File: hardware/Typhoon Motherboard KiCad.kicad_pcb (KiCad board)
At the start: 2 copper layers, 65.7 x 44.9 mm, 57 parts, among them J1 Conn_01x04_Pin, J10 USB_C_Receptacle_USB2.0, J11 Conn_01x02_Pin, J12 Conn_01x02_Pin, J13 Conn_01x02_Pin, J14 Conn_01x02_Pin, J15 Conn_01x02_Pin, J16 Conn_01x02_Pin, J2 Conn_02x03_Odd_Even, J3 Conn_01x04_Pin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

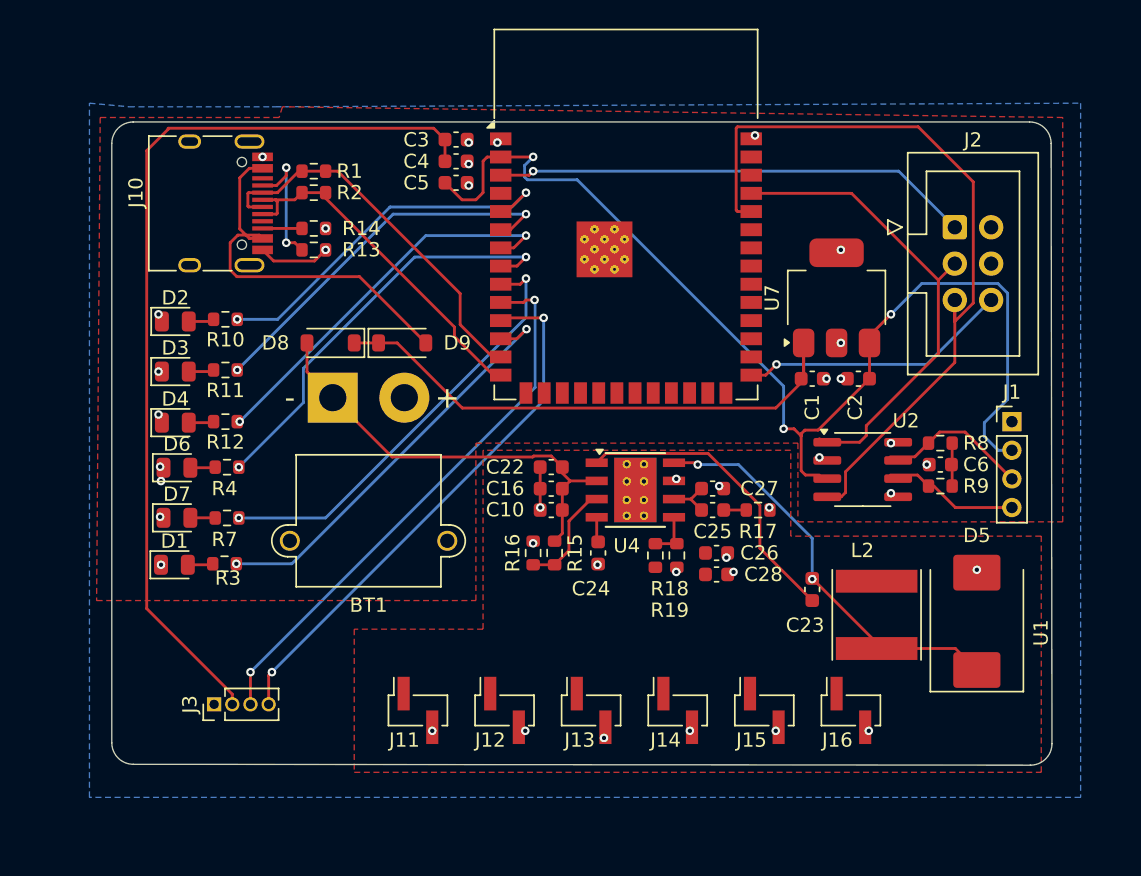
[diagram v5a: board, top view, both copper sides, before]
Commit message: Added mounting holes
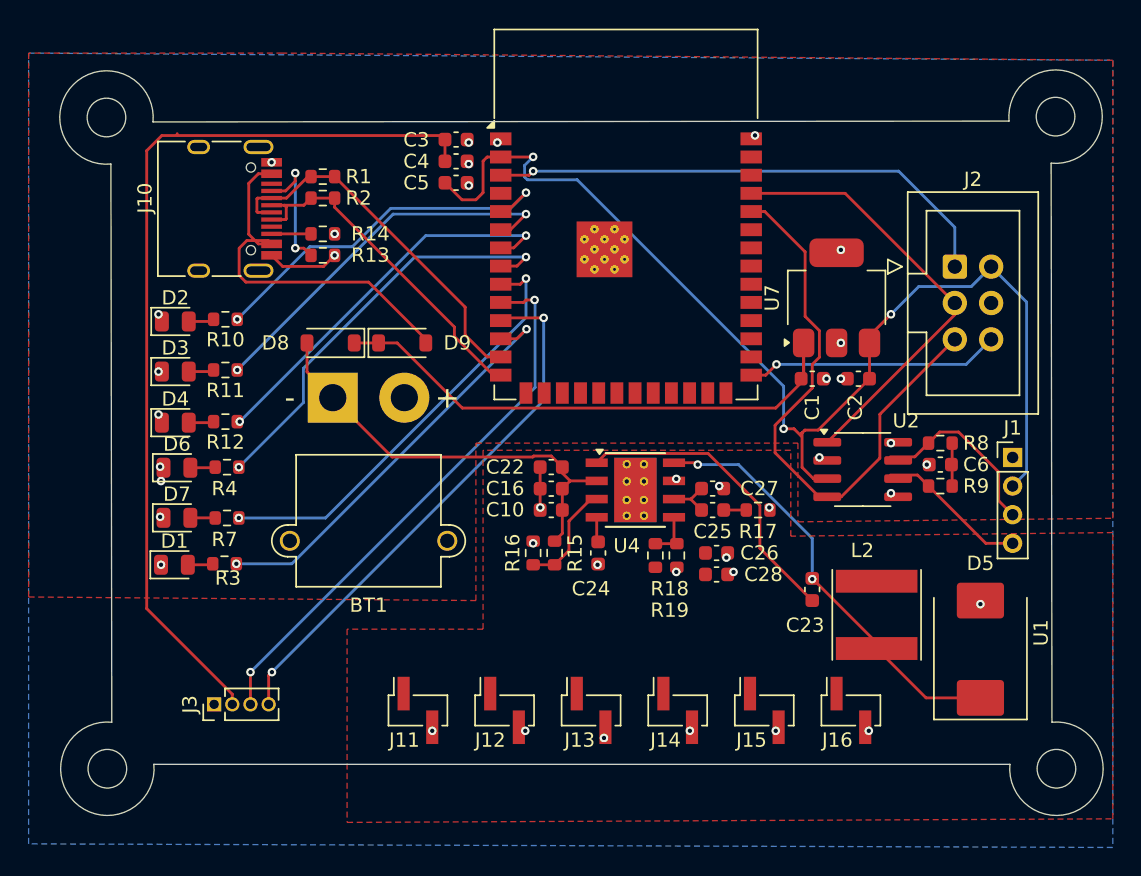
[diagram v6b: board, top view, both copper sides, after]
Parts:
- added H1: M2.5, MountingHole:MountingHole_2.7mm_M2.5, F.Cu at (105.2, 79.3)
- added H1: M2.5, MountingHole:MountingHole_2.7mm_M2.5, F.Cu at (171.5, 79.2)
- added H1: M2.5, MountingHole:MountingHole_2.7mm_M2.5, F.Cu at (105.2, 124.8)
- added H1: M2.5, MountingHole:MountingHole_2.7mm_M2.5, F.Cu at (171.6, 124.7)
- moved J2 2.75 mm to (164.5, 89.7)
- moved J1 2.50 mm to (168.5, 103.0)
- moved D5 1.97 mm to (166.2, 116.4)
- moved J10 0.74 mm to (112.7, 85.6)
- moved R1 0.74 mm to (120.3, 83.4)
- moved R13 0.74 mm to (120.3, 88.9)
- moved R14 0.74 mm to (120.3, 87.4)
- moved R2 0.74 mm to (120.3, 84.9)
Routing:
- net /Prog/TypeC_{RX}: track 54.8 -> 40.9 mm
- net +3.3V: track 141.7 -> 144.8 mm
- net /Prog/TypeC_{TX}: track 33.7 -> 30.8 mm
- net /EN: track 33.5 -> 36.2 mm
- net /CAN_{H}: track 10.6 -> 12.8 mm
- net /IO0: track 18.9 -> 17.8 mm
- net /CAN_{L}: track 9.44 -> 10.5 mm
- net Net-(D5-K): track 29.1 -> 30.1 mm
- net /D-: track 26.9 -> 26.0 mm
- net VDC: track 27.6 -> 26.9 mm
- net /D+: track 24.8 -> 24.1 mm
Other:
- board size 65.7 x 44.9 mm -> 72.9 x 52.1 mm

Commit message: Updated header (NOT FINAL)
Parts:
- removed the H1 at (105.2, 79.3)
- removed the H1 at (171.5, 79.2)
- removed the H1 at (105.2, 124.8)
- removed the H1 at (171.6, 124.7)
- added H1: M2.5, MountingHole:MountingHole_2.7mm_M2.5, F.Cu at (171.5, 124.8)
- added H2: M2.5, MountingHole:MountingHole_2.7mm_M2.5, F.Cu at (105.2, 124.8)
- added H3: M2.5, MountingHole:MountingHole_2.7mm_M2.5, F.Cu at (171.5, 79.2)
- added H4: M2.5, MountingHole:MountingHole_2.7mm_M2.5, F.Cu at (105.2, 79.2)
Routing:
- net /D+: track 24.1 -> 25.6 mm
- net GND: vias 39 -> 46

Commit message: Final Edit
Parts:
- moved J10 5.71 mm to (107.7, 88.4)
- moved R1 5.71 mm to (115.3, 86.1)
- moved R13 5.71 mm to (115.3, 91.6)
- moved R14 5.71 mm to (115.3, 90.1)
- moved R2 5.71 mm to (115.3, 87.6)
- moved J3 2.57 mm to (115.0, 121.5)
- moved D1 2.30 mm to (109.4, 112.8)
- moved D2 2.30 mm to (109.5, 95.8)
- moved D3 2.30 mm to (109.5, 99.2)
- moved D4 2.30 mm to (109.5, 102.8)
- moved D6 2.30 mm to (109.6, 106.0)
- moved D7 2.30 mm to (109.6, 109.5)
- moved R10 2.30 mm to (113.0, 95.6)
- moved R11 2.30 mm to (113.0, 99.1)
- moved R12 2.30 mm to (113.0, 102.8)
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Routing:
- net +3.3V: track 144.8 -> 90.0 mm, vias 3 -> 4
- net VDC: track 26.9 -> 30.9 mm
- net /D-: track 26.1 -> 29.1 mm
- net /D+: track 25.6 -> 28.6 mm
- net GND: track 8.06 -> 11.0 mm
- net /LED_{4}: track 29.1 -> 31.4 mm
- net /LED_{3}: track 27.5 -> 29.6 mm
- net /LED_{6}: track 30.5 -> 32.2 mm
- net /LED_{5}: track 29.6 -> 31.1 mm
- net /LED_{2}: track 26.9 -> 28.3 mm
- net /LED_{1}: track 26.2 -> 27.6 mm
- net /Mother_{TX}: track 38.9 -> 40.2 mm, vias 2 -> 1
- net /Mother_{RX}: track 38.0 -> 38.4 mm, vias 2 -> 1
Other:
- board size 72.9 x 52.1 mm -> 73.5 x 52.8 mm
- board text added: "3.3V"
- board text added: "3.3V GND"
- board text added: "5V to 3.3V"
- board text added: "CAN Transceiver"
- board text added: "CAN_{H}"
- board text added: "CAN_{L}"
- board text added: "Can be used as central power source"
- board text added: "Central Power Source Mode"
- board text added: "GND"
- board text added: "LED_{1}"
- board text added: "LED_{2}"
- board text added: "LED_{3}"
- board text added: "LED_{4}"
- board text added: "LED_{5}"
- board text added: "LED_{6}"
- board text added: "Programming Header"
- board text added: "Telemetry"
- board text added: "Type C"
- board text added: "Typhoon Motherboard Designed by Jaden Stanshall, Justin Lo"
